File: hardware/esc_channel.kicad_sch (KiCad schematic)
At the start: 17 parts, among them Q32 AGM210MAP, Q33 AGM210MAP, Q34 AGM210MAP, U7 EFM8BB51F16I

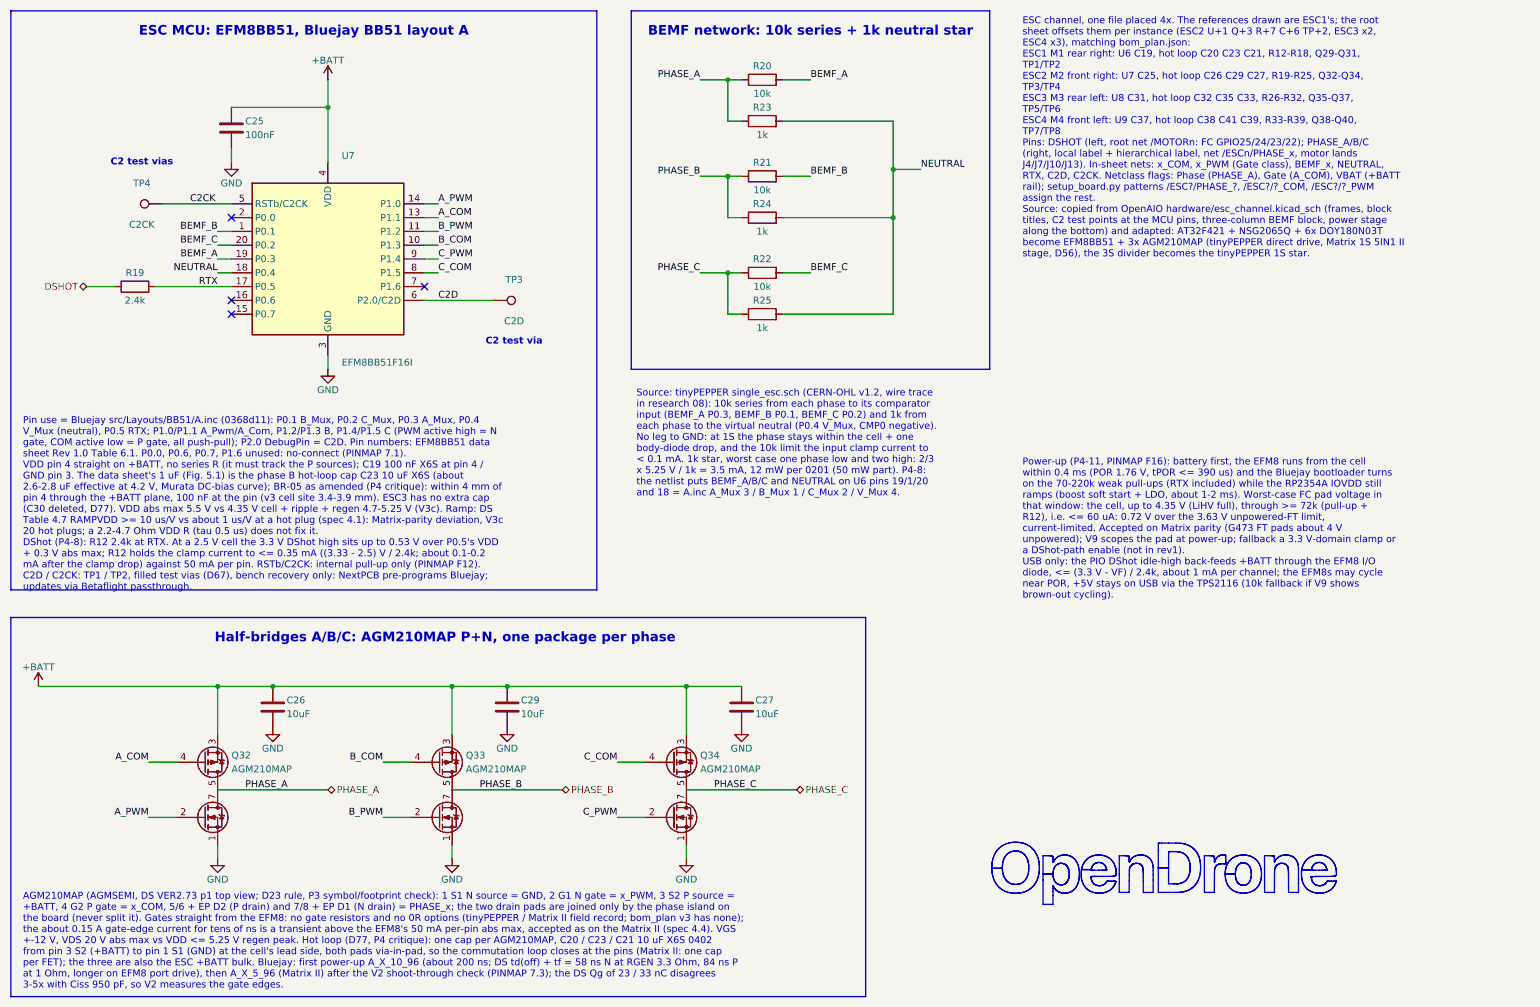
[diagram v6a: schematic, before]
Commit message: wip: D108 per-FET 22 uF 0603 caps in the schematic (verification running)
Co-Authored-By: Claude Opus 5.5 <noreply@anthropic.com>
Claude-Session: https://claude.ai/code/session_01RFaS5jnC9tnPam9GBgmGnG
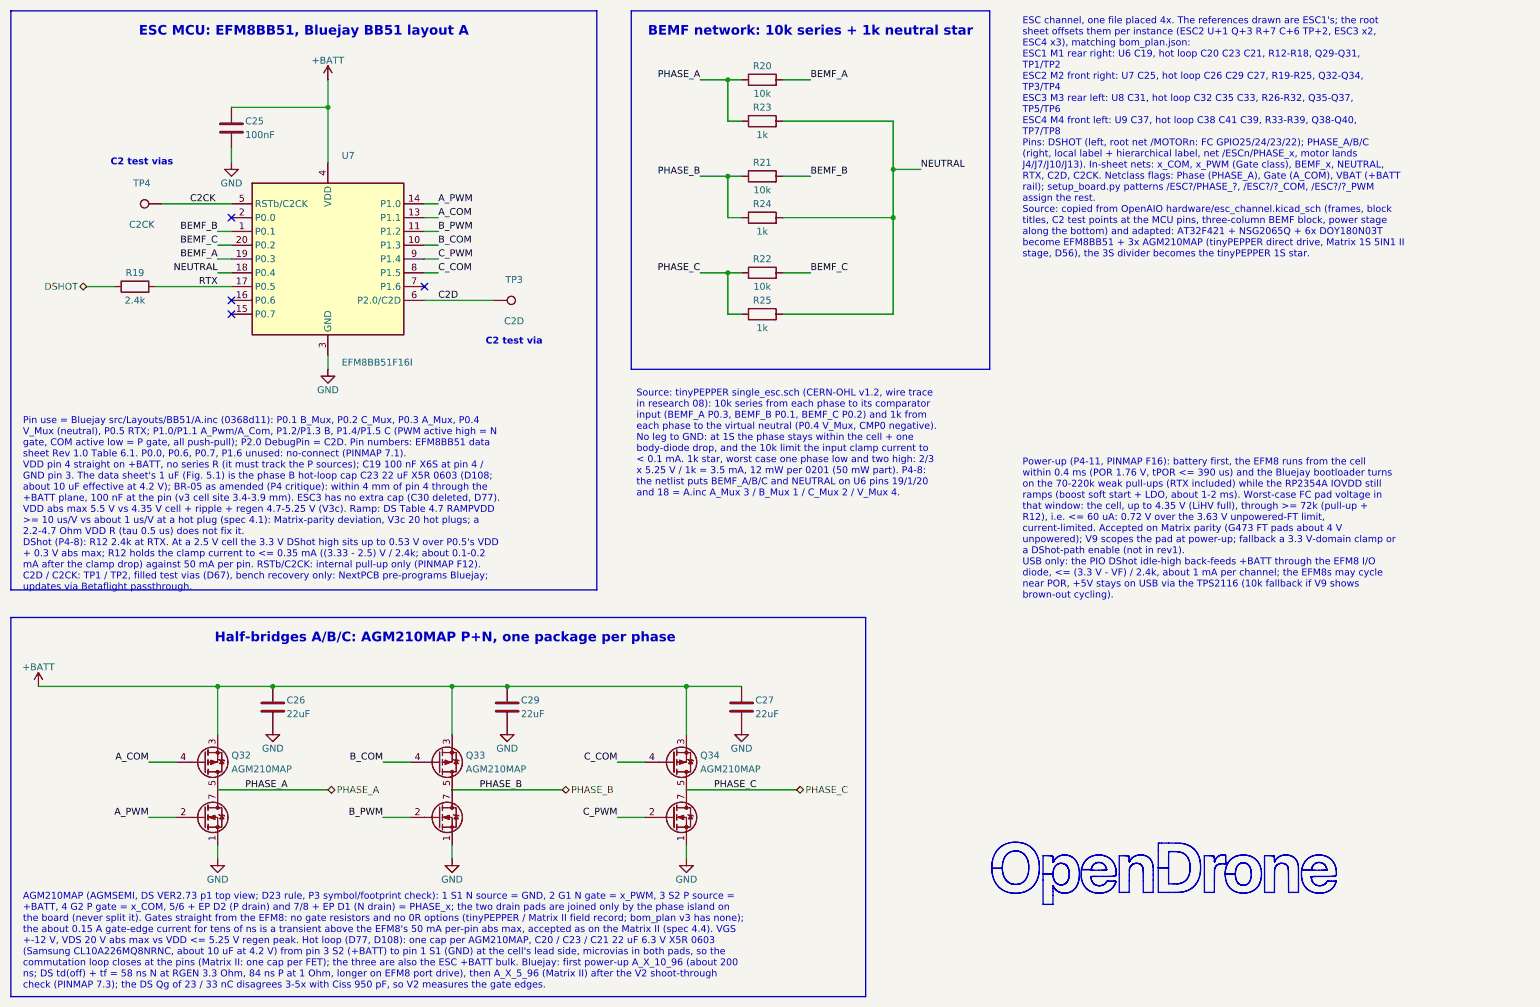
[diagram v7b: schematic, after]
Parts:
- C26, C27, C29: value 10uF -> 22uF; footprint lib:C_0402_1005Metric_W -> lib:C_0603_1608Metric_W; LCSC C237279 -> C59461; MPN GRM155C80J106ME11D -> CL10A226MQ8NRNC; Manufacturer Murata -> Samsung Electro-Mechanics
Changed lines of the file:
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@@
 		)
 	)
-	(text_box "AGM210MAP (AGMSEMI, DS VER2.73 p1 top view; D23 rule, P3 symbol/footprint check): 1 S1 N source = GND, 2 G1 N gate = x_PWM, 3 S2 P source = +BATT, 4 G2 P gate = x_COM, 5/6 + EP D2 (P drain) and 7/8 + EP D1 (N drain) = PHASE_x; the two drain pads are joined only by the phase island on the board (never split it). Gates straight from the EFM8: no gate resistors and no 0R options (tinyPEPPER / Matrix II field record; bom_plan v3 has none); the about 0.15 A gate-edge current for tens of ns is a transient above the EFM8's 50 mA per-pin abs max, accepted as on the Matrix II (spec 4.4). VGS +-12 V, VDS 20 V abs max vs VDD <= 5.25 V regen peak. Hot loop (D77, P4 critique): one cap per AGM210MAP, C20 / C23 / C21 10 uF X6S 0402 from pin 3 S2 (+BATT) to pin 1 S1 (GND) at the cell's lead side, both pads via-in-pad, so the commutation loop closes at the pins (Matrix II: one cap per FET); the three are also the ESC +BATT bulk. Bluejay: first power-up A_X_10_96 (about 200 ns; DS td(off) + tf = 58 ns N at RGEN 3.3 Ohm, 84 ns P at 1 Ohm, longer on EFM8 port drive), then A_X_5_96 (Matrix II) after the V2 shoot-through check (PINMAP 7.3); the DS Qg of 23 / 33 nC disagrees 3-5x with Ciss 950 pF, so V2 measures the gate edges."
+	(text_box "AGM210MAP (AGMSEMI, DS VER2.73 p1 top view; D23 rule, P3 symbol/footprint check): 1 S1 N source = GND, 2 G1 N gate = x_PWM, 3 S2 P source = +BATT, 4 G2 P gate = x_COM, 5/6 + EP D2 (P drain) and 7/8 + EP D1 (N drain) = PHASE_x; the two drain pads are joined only by the phase island on the board (never split it). Gates straight from the EFM8: no gate resistors and no 0R options (tinyPEPPER / Matrix II field record; bom_plan v3 has none); the about 0.15 A gate-edge current for tens of ns is a transient above the EFM8's 50 mA per-pin abs max, accepted as on the Matrix II (spec 4.4). VGS +-12 V, VDS 20 V abs max vs VDD <= 5.25 V regen peak. Hot loop (D77, D108): one cap per AGM210MAP, C20 / C23 / C21 22 uF 6.3 V X5R 0603 (Samsung CL10A226MQ8NRNC, about 10 uF at 4.2 V) from pin 3 S2 (+BATT) to pin 1 S1 (GND) at the cell's lead side, microvias in both pads, so the commutation loop closes at the pins (Matrix II: one cap per FET); the three are also the ESC +BATT bulk. Bluejay: first power-up A_X_10_96 (about 200 ns; DS td(off) + tf = 58 ns N at RGEN 3.3 Ohm, 84 ns P at 1 Ohm, longer on EFM8 port drive), then A_X_5_96 (Matrix II) after the V2 shoot-through check (PINMAP 7.3); the DS Qg of 23 / 33 nC disagrees 3-5x with Ciss 950 pF, so V2 measures the gate edges."
 		(exclude_from_sim no)
 		(at 19.05 176.53 0)
@@
 		)
 	)
-	(text_box "Pin use = Bluejay src/Layouts/BB51/A.inc (0368d11): P0.1 B_Mux, P0.2 C_Mux, P0.3 A_Mux, P0.4 V_Mux (neutral), P0.5 RTX; P1.0/P1.1 A_Pwm/A_Com, P1.2/P1.3 B, P1.4/P1.5 C (PWM active high = N gate, COM active low = P gate, all push-pull); P2.0 DebugPin = C2D. Pin numbers: EFM8BB51 data sheet Rev 1.0 Table 6.1. P0.0, P0.6, P0.7, P1.6 unused: no-connect (PINMAP 7.1).\nVDD pin 4 straight on +BATT, no series R (it must track the P sources); C19 100 nF X6S at pin 4 / GND pin 3. The data sheet's 1 uF (Fig. 5.1) is the phase B hot-loop cap C23 10 uF X6S (about 2.6-2.8 uF effective at 4.2 V, Murata DC-bias curve); BR-05 as amended (P4 critique): within 4 mm of pin 4 through the +BATT plane, 100 nF at the pin (v3 cell site 3.4-3.9 mm). ESC3 has no extra cap (C30 deleted, D77). VDD abs max 5.5 V vs 4.35 V cell + ripple + regen 4.7-5.25 V (V3c). Ramp: DS Table 4.7 RAMPVDD >= 10 us/V vs about 1 us/V at a hot plug (spec 4.1): Matrix-parity deviation, V3c 20 hot plugs; a 2.2-4.7 Ohm VDD R (tau 0.5 us) does not fix it.\nDShot (P4-8): R12 2.4k at RTX. At a 2.5 V cell the 3.3 V DShot high sits up to 0.53 V over P0.5's VDD + 0.3 V abs max; R12 holds the clamp current to <= 0.35 mA ((3.33 - 2.5) V / 2.4k; about 0.1-0.2 mA after the clamp drop) against 50 mA per pin. RSTb/C2CK: internal pull-up only (PINMAP F12).\nC2D / C2CK: TP1 / TP2, filled test vias (D67), bench recovery only: NextPCB pre-programs Bluejay; updates via Betaflight passthrough."
+	(text_box "Pin use = Bluejay src/Layouts/BB51/A.inc (0368d11): P0.1 B_Mux, P0.2 C_Mux, P0.3 A_Mux, P0.4 V_Mux (neutral), P0.5 RTX; P1.0/P1.1 A_Pwm/A_Com, P1.2/P1.3 B, P1.4/P1.5 C (PWM active high = N gate, COM active low = P gate, all push-pull); P2.0 DebugPin = C2D. Pin numbers: EFM8BB51 data sheet Rev 1.0 Table 6.1. P0.0, P0.6, P0.7, P1.6 unused: no-connect (PINMAP 7.1).\nVDD pin 4 straight on +BATT, no series R (it must track the P sources); C19 100 nF X6S at pin 4 / GND pin 3. The data sheet's 1 uF (Fig. 5.1) is the phase B hot-loop cap C23 22 uF X5R 0603 (D108; about 10 uF effective at 4.2 V); BR-05 as amended (P4 critique): within 4 mm of pin 4 through the +BATT plane, 100 nF at the pin (v3 cell site 3.4-3.9 mm). ESC3 has no extra cap (C30 deleted, D77). VDD abs max 5.5 V vs 4.35 V cell + ripple + regen 4.7-5.25 V (V3c). Ramp: DS Table 4.7 RAMPVDD >= 10 us/V vs about 1 us/V at a hot plug (spec 4.1): Matrix-parity deviation, V3c 20 hot plugs; a 2.2-4.7 Ohm VDD R (tau 0.5 us) does not fix it.\nDShot (P4-8): R12 2.4k at RTX. At a 2.5 V cell the 3.3 V DShot high sits up to 0.53 V over P0.5's VDD + 0.3 V abs max; R12 holds the clamp current to <= 0.35 mA ((3.33 - 2.5) V / 2.4k; about 0.1-0.2 mA after the clamp drop) against 50 mA per pin. RSTb/C2CK: internal pull-up only (PINMAP F12).\nC2D / C2CK: TP1 / TP2, filled test vias (D67), bench recovery only: NextPCB pre-programs Bluejay; updates via Betaflight passthrough."
 		(exclude_from_sim no)
 		(at 19.05 88.9 0)
@@
 			)
 		)
-		(property "Value" "10uF"
+		(property "Value" "22uF"
 			(at 68.58 144.78 0)
 			(show_name no)
@@
 			)
 		)
-		(property "Footprint" "lib:C_0402_1005Metric_W"
+		(property "Footprint" "lib:C_0603_1608Metric_W"
 			(at 66.04 143.51 0)
 			(hide yes)
@@
 			)
 		)
-		(property "LCSC" "C237279"
+		(property "LCSC" "C59461"
 			(at 66.04 143.51 0)
 			(hide yes)
@@
 			)
 		)
-		(property "MPN" "GRM155C80J106ME11D"
+		(property "MPN" "CL10A226MQ8NRNC"
 			(at 66.04 143.51 0)
 			(hide yes)
@@
 			)
 		)
-		(property "Manufacturer" "Murata"
+		(property "Manufacturer" "Samsung Electro-Mechanics"
 			(at 66.04 143.51 0)
 			(hide yes)
@@
 			)
 		)
-		(property "Value" "10uF"
+		(property "Value" "22uF"
 			(at 154.94 144.78 0)
 			(show_name no)
@@
 			)
 		)
-		(property "Footprint" "lib:C_0402_1005Metric_W"
+		(property "Footprint" "lib:C_0603_1608Metric_W"
 			(at 152.4 143.51 0)
 			(hide yes)
@@
 			)
 		)
-		(property "LCSC" "C237279"
+		(property "LCSC" "C59461"
 			(at 152.4 143.51 0)
 			(hide yes)
@@
 			)
 		)
-		(property "MPN" "GRM155C80J106ME11D"
+		(property "MPN" "CL10A226MQ8NRNC"
 			(at 152.4 143.51 0)
 			(hide yes)
@@
 			)
 		)
-		(property "Manufacturer" "Murata"
+		(property "Manufacturer" "Samsung Electro-Mechanics"
 			(at 152.4 143.51 0)
 			(hide yes)
@@
 			)
 		)
-		(property "Value" "10uF"
+		(property "Value" "22uF"
 			(at 111.76 144.78 0)
 			(show_name no)
@@
 			)
 		)
-		(property "Footprint" "lib:C_0402_1005Metric_W"
+		(property "Footprint" "lib:C_0603_1608Metric_W"
 			(at 109.22 143.51 0)
 			(hide yes)
@@
 			)
 		)
-		(property "LCSC" "C237279"
+		(property "LCSC" "C59461"
 			(at 109.22 143.51 0)
 			(hide yes)
@@
 			)
 		)
-		(property "MPN" "GRM155C80J106ME11D"
+		(property "MPN" "CL10A226MQ8NRNC"
 			(at 109.22 143.51 0)
 			(hide yes)
@@
 			)
 		)
-		(property "Manufacturer" "Murata"
+		(property "Manufacturer" "Samsung Electro-Mechanics"
 			(at 109.22 143.51 0)
 			(hide yes)
